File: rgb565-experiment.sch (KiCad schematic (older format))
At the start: 32 parts, among them J1 ST_SHIFTER_SOCKET, SW1 SW_SPDT, U1 74HC00, U2 ST_SHIFTER, U3 ST_SHIFTER, U4 74HC245, U5 74LS257, U6 74HC245

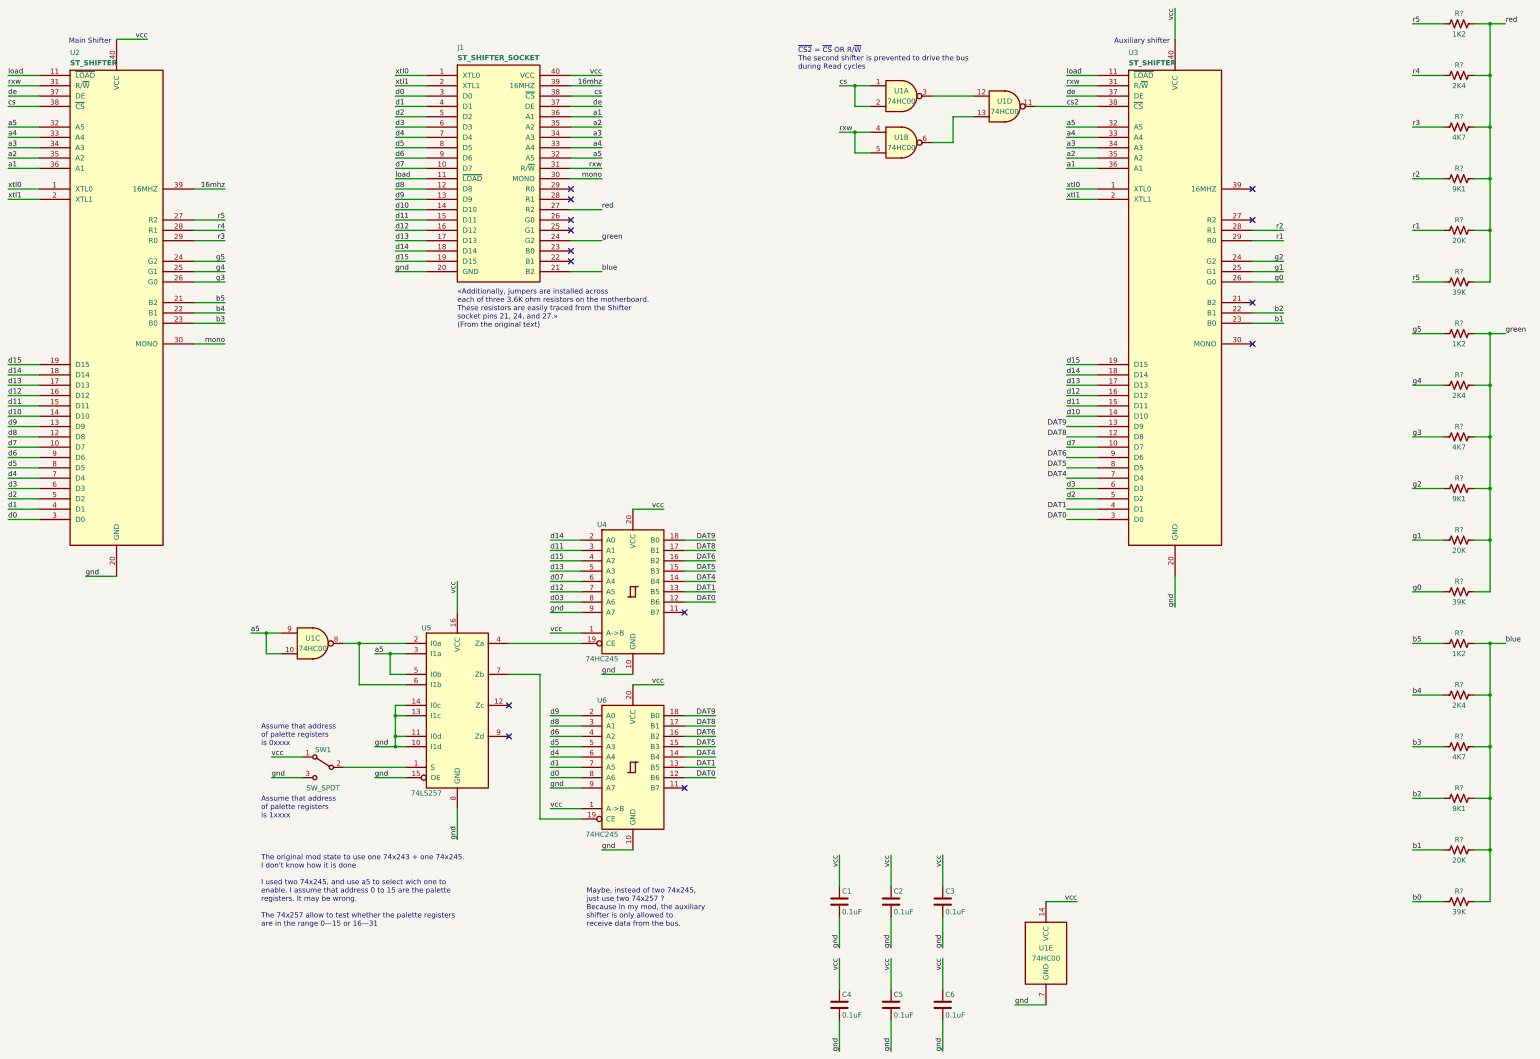
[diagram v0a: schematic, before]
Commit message: fixes some ERC warning
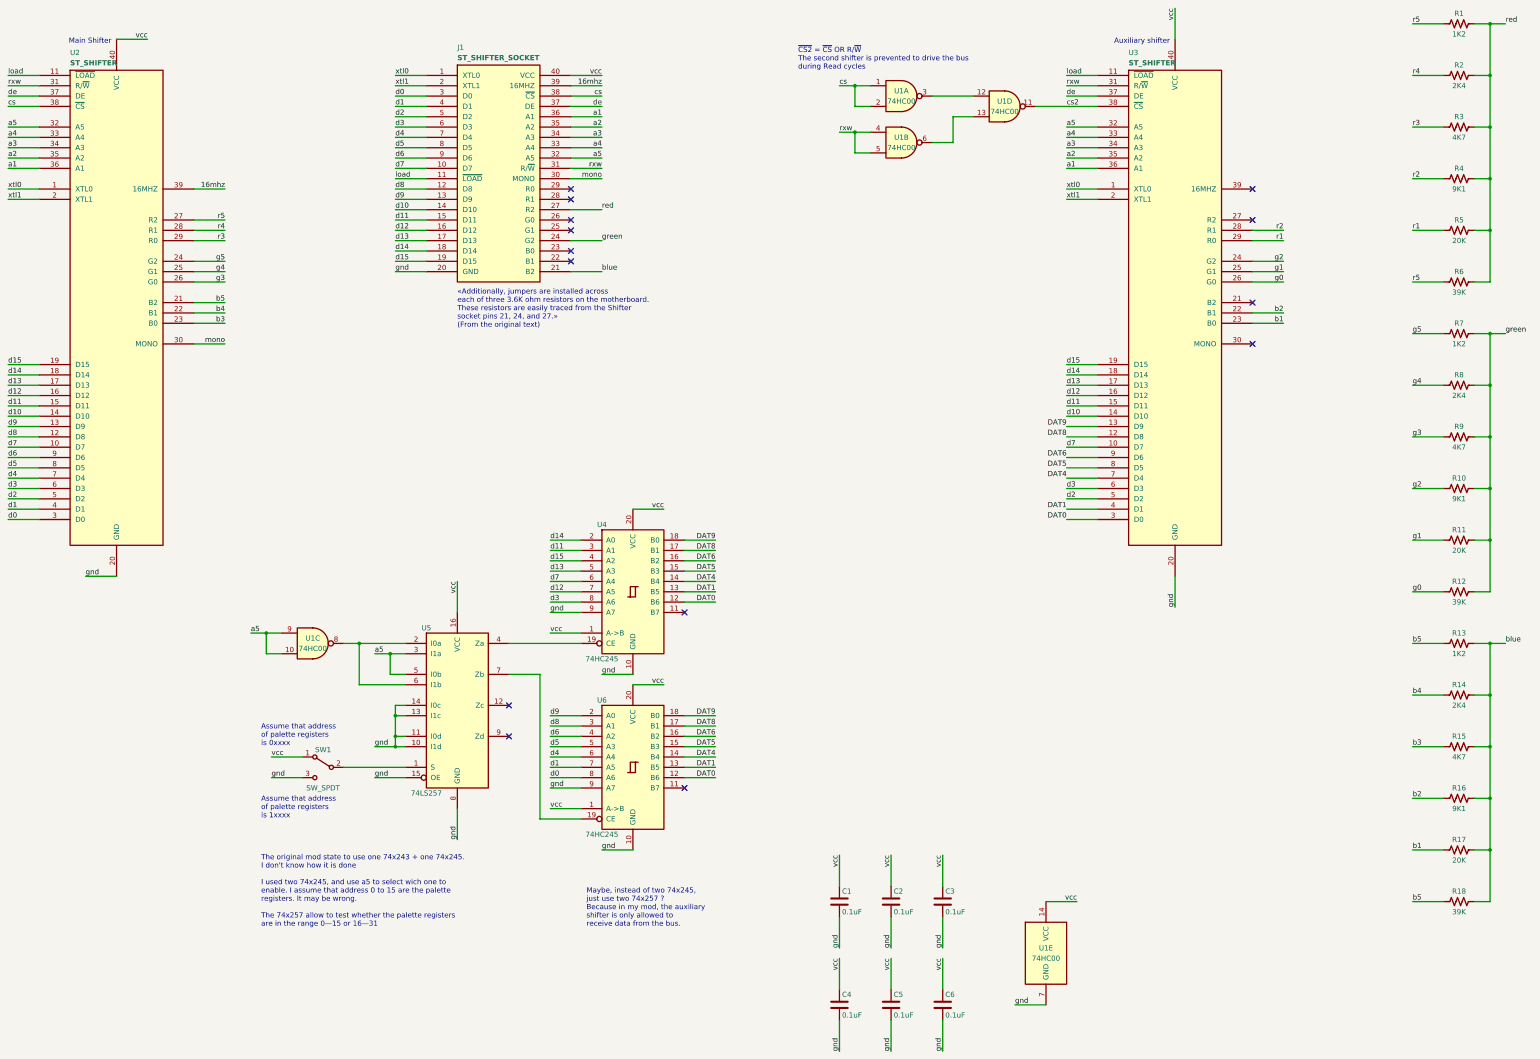
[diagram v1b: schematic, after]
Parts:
- gave numbers to parts that had none: 18
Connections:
- net b0 is gone; now on net b5: R18.1
- net d03 is gone; now on net d3: U4.8 (A6)
- net d07 is gone; now on net d7: U4.6 (A4)
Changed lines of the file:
@@
 d13
 Text Label 6200 6400 0    50   ~ 0
-d07
+d7
 Text Label 6200 6500 0    50   ~ 0
 d12
 Text Label 6200 6600 0    50   ~ 0
-d03
+d3
 Text Label 6200 7700 0    50   ~ 0
 d9
@@
 	9000 9350 9000 9050
 $Comp
-L Device:R_US R?
+L Device:R_US R1
 U 1 1 61BB4DC8
 P 15000 1000
-F 0 "R?" V 15100 1000 50  0000 C CNN
+F 0 "R1" V 15100 1000 50  0000 C CNN
 F 1 "1K2" V 14900 1000 50  0000 C CNN
 F 2 "" V 15040 990 50  0001 C CNN
@@
 $EndComp
 $Comp
-L Device:R_US R?
+L Device:R_US R2
 U 1 1 61BD219E
 P 15000 1500
-F 0 "R?" V 15100 1500 50  0000 C CNN
+F 0 "R2" V 15100 1500 50  0000 C CNN
 F 1 "2K4" V 14900 1500 50  0000 C CNN
 F 2 "" V 15040 1490 50  0001 C CNN
@@
 $EndComp
 $Comp
-L Device:R_US R?
+L Device:R_US R3
 U 1 1 61BD3284
 P 15000 2000
-F 0 "R?" V 15100 2000 50  0000 C CNN
+F 0 "R3" V 15100 2000 50  0000 C CNN
 F 1 "4K7" V 14900 2000 50  0000 C CNN
 F 2 "" V 15040 1990 50  0001 C CNN
@@
 $EndComp
 $Comp
-L Device:R_US R?
+L Device:R_US R4
 U 1 1 61BD3A49
 P 15000 2500
-F 0 "R?" V 15100 2500 50  0000 C CNN
+F 0 "R4" V 15100 2500 50  0000 C CNN
 F 1 "9K1" V 14900 2500 50  0000 C CNN
 F 2 "" V 15040 2490 50  0001 C CNN
@@
 $EndComp
 $Comp
-L Device:R_US R?
+L Device:R_US R5
 U 1 1 61BD4323
 P 15000 3000
-F 0 "R?" V 15100 3000 50  0000 C CNN
+F 0 "R5" V 15100 3000 50  0000 C CNN
 F 1 "20K" V 14900 3000 50  0000 C CNN
 F 2 "" V 15040 2990 50  0001 C CNN
@@
 $EndComp
 $Comp
-L Device:R_US R?
+L Device:R_US R6
 U 1 1 61BD4732
 P 15000 3500
-F 0 "R?" V 15100 3500 50  0000 C CNN
+F 0 "R6" V 15100 3500 50  0000 C CNN
 F 1 "39K" V 14900 3500 50  0000 C CNN
 F 2 "" V 15040 3490 50  0001 C CNN
@@
 red
 $Comp
-L Device:R_US R?
+L Device:R_US R7
 U 1 1 61C691D3
 P 15000 4000
-F 0 "R?" V 15100 4000 50  0000 C CNN
+F 0 "R7" V 15100 4000 50  0000 C CNN
 F 1 "1K2" V 14900 4000 50  0000 C CNN
 F 2 "" V 15040 3990 50  0001 C CNN
@@
 $EndComp
 $Comp
-L Device:R_US R?
+L Device:R_US R8
 U 1 1 61C691D9
 P 15000 4500
-F 0 "R?" V 15100 4500 50  0000 C CNN
+F 0 "R8" V 15100 4500 50  0000 C CNN
 F 1 "2K4" V 14900 4500 50  0000 C CNN
 F 2 "" V 15040 4490 50  0001 C CNN
@@
 $EndComp
 $Comp
-L Device:R_US R?
+L Device:R_US R9
 U 1 1 61C691DF
 P 15000 5000
-F 0 "R?" V 15100 5000 50  0000 C CNN
+F 0 "R9" V 15100 5000 50  0000 C CNN
 F 1 "4K7" V 14900 5000 50  0000 C CNN
 F 2 "" V 15040 4990 50  0001 C CNN
@@
 $EndComp
 $Comp
-L Device:R_US R?
+L Device:R_US R10
 U 1 1 61C691E5
 P 15000 5500
-F 0 "R?" V 15100 5500 50  0000 C CNN
+F 0 "R10" V 15100 5500 50  0000 C CNN
 F 1 "9K1" V 14900 5500 50  0000 C CNN
 F 2 "" V 15040 5490 50  0001 C CNN
@@
 $EndComp
 $Comp
-L Device:R_US R?
+L Device:R_US R11
 U 1 1 61C691EB
 P 15000 6000
-F 0 "R?" V 15100 6000 50  0000 C CNN
+F 0 "R11" V 15100 6000 50  0000 C CNN
 F 1 "20K" V 14900 6000 50  0000 C CNN
 F 2 "" V 15040 5990 50  0001 C CNN
@@
 $EndComp
 $Comp
-L Device:R_US R?
+L Device:R_US R12
 U 1 1 61C691F1
 P 15000 6500
-F 0 "R?" V 15100 6500 50  0000 C CNN
+F 0 "R12" V 15100 6500 50  0000 C CNN
 F 1 "39K" V 14900 6500 50  0000 C CNN
 F 2 "" V 15040 6490 50  0001 C CNN
@@
 green
 $Comp
-L Device:R_US R?
+L Device:R_US R13
 U 1 1 61C89607
 P 15000 7000
-F 0 "R?" V 15100 7000 50  0000 C CNN
+F 0 "R13" V 15100 7000 50  0000 C CNN
 F 1 "1K2" V 14900 7000 50  0000 C CNN
 F 2 "" V 15040 6990 50  0001 C CNN
@@
 $EndComp
 $Comp
-L Device:R_US R?
+L Device:R_US R14
 U 1 1 61C8960D
 P 15000 7500
-F 0 "R?" V 15100 7500 50  0000 C CNN
+F 0 "R14" V 15100 7500 50  0000 C CNN
 F 1 "2K4" V 14900 7500 50  0000 C CNN
 F 2 "" V 15040 7490 50  0001 C CNN
@@
 $EndComp
 $Comp
-L Device:R_US R?
+L Device:R_US R15
 U 1 1 61C89613
 P 15000 8000
-F 0 "R?" V 15100 8000 50  0000 C CNN
+F 0 "R15" V 15100 8000 50  0000 C CNN
 F 1 "4K7" V 14900 8000 50  0000 C CNN
 F 2 "" V 15040 7990 50  0001 C CNN
@@
 $EndComp
 $Comp
-L Device:R_US R?
+L Device:R_US R16
 U 1 1 61C89619
 P 15000 8500
-F 0 "R?" V 15100 8500 50  0000 C CNN
+F 0 "R16" V 15100 8500 50  0000 C CNN
 F 1 "9K1" V 14900 8500 50  0000 C CNN
 F 2 "" V 15040 8490 50  0001 C CNN
@@
 $EndComp
 $Comp
-L Device:R_US R?
+L Device:R_US R17
 U 1 1 61C8961F
 P 15000 9000
-F 0 "R?" V 15100 9000 50  0000 C CNN
+F 0 "R17" V 15100 9000 50  0000 C CNN
 F 1 "20K" V 14900 9000 50  0000 C CNN
 F 2 "" V 15040 8990 50  0001 C CNN
@@
 $EndComp
 $Comp
-L Device:R_US R?
+L Device:R_US R18
 U 1 1 61C89625
 P 15000 9500
-F 0 "R?" V 15100 9500 50  0000 C CNN
+F 0 "R18" V 15100 9500 50  0000 C CNN
 F 1 "39K" V 14900 9500 50  0000 C CNN
 F 2 "" V 15040 9490 50  0001 C CNN
@@
 b1
 Text Label 14550 9500 0    50   ~ 0
-b0
+b5
 Text Label 15450 7000 0    50   ~ 0
 blue
